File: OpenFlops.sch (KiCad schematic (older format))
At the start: 74 parts, among them P1 FLOPPY_CONN, P2 POWER_INPUT, P3 USB_A_FEMALE, P4 PROG_PORT, P5 JUMPERS, P6 ENCODER_PORT, P7 DISPLAY_PORT, Q1 MOS_N_GSD, Q2 MOS_N_GSD, Q3 MOS_N_GSD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

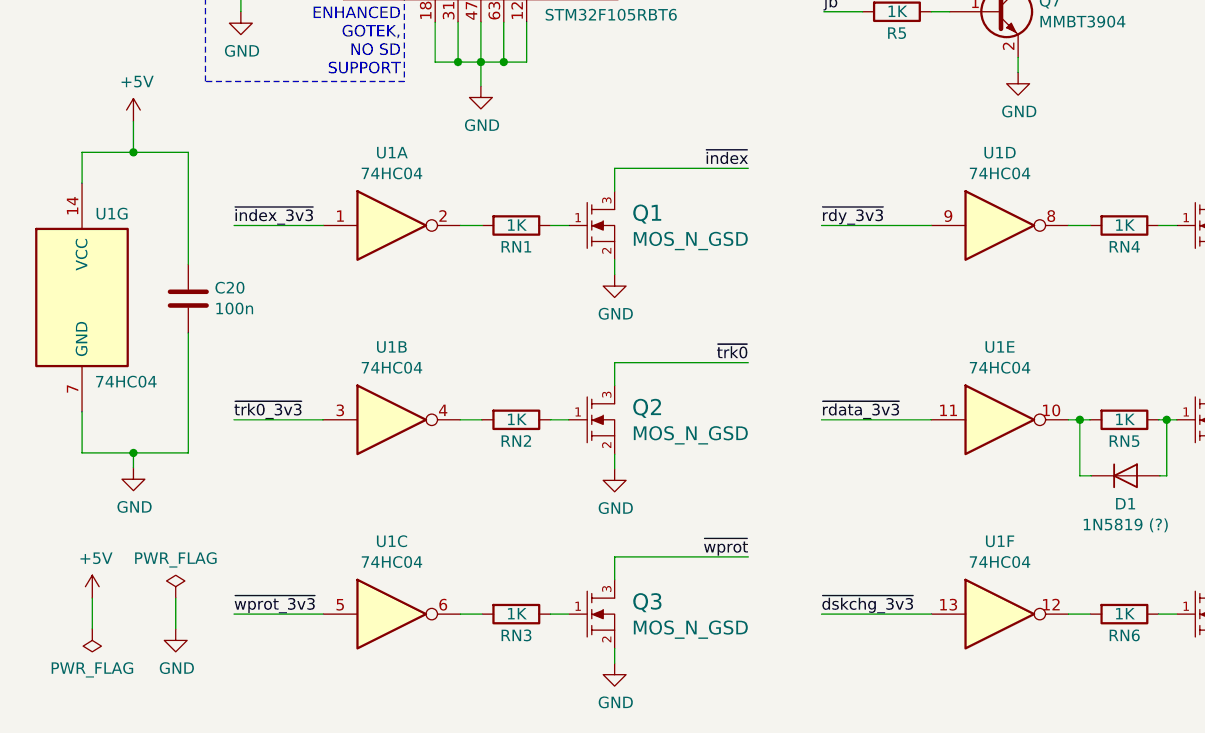
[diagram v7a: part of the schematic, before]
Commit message: 74HC04 -> 74HCT04
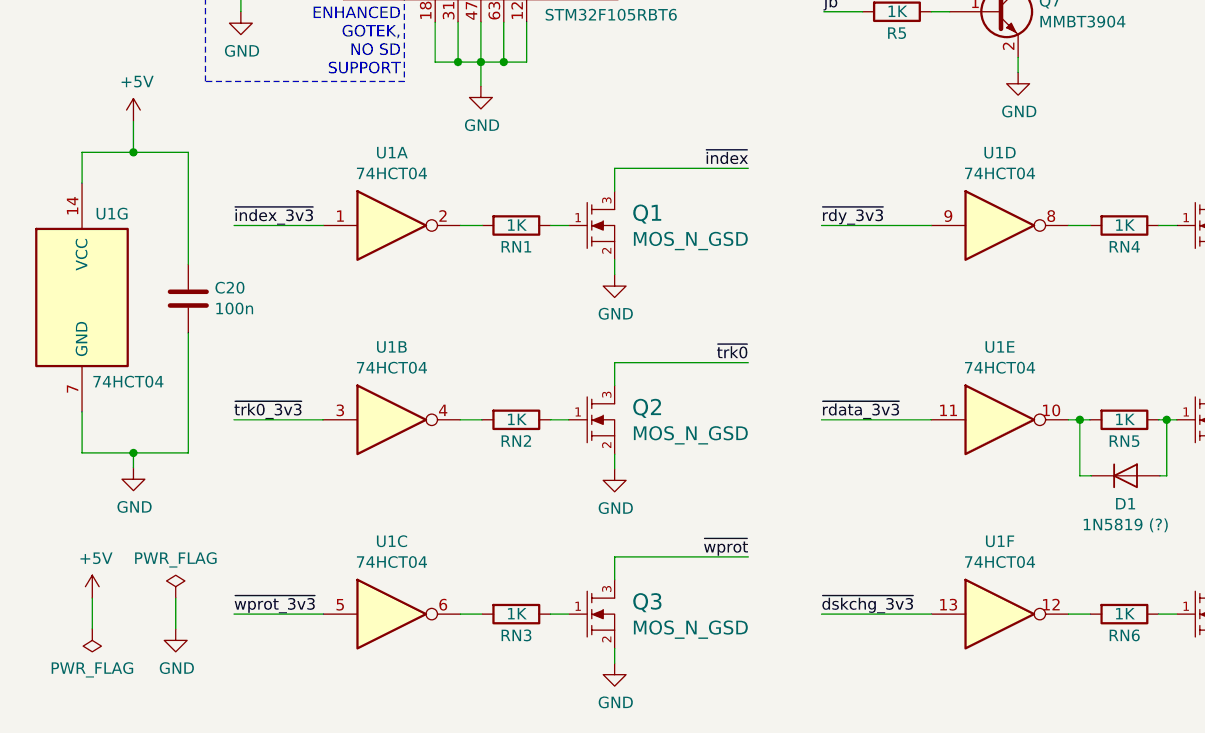
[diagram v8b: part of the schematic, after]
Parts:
- U1: value 74HC04 -> 74HCT04
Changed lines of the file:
@@
 P 2165 5590
 F 0 "U1" H 2165 5907 50  0000 C CNN
-F 1 "74HC04" H 2165 5816 50  0000 C CNN
+F 1 "74HCT04" H 2165 5816 50  0000 C CNN
 F 2 "Package_SO:SOIC-14_3.9x8.7mm_P1.27mm" H 2165 5590 50  0001 C CNN
 F 3 "https://assets.nexperia.com/documents/data-sheet/74HC_HCT04.pdf" H 2165 5590 50  0001 C CNN
@@
 P 2165 7290
 F 0 "U1" H 2165 7607 50  0000 C CNN
-F 1 "74HC04" H 2165 7516 50  0000 C CNN
+F 1 "74HCT04" H 2165 7516 50  0000 C CNN
 F 2 "Package_SO:SOIC-14_3.9x8.7mm_P1.27mm" H 2165 7290 50  0001 C CNN
 F 3 "https://assets.nexperia.com/documents/data-sheet/74HC_HCT04.pdf" H 2165 7290 50  0001 C CNN
@@
 P 4825 5590
 F 0 "U1" H 4825 5907 50  0000 C CNN
-F 1 "74HC04" H 4825 5816 50  0000 C CNN
+F 1 "74HCT04" H 4825 5816 50  0000 C CNN
 F 2 "Package_SO:SOIC-14_3.9x8.7mm_P1.27mm" H 4825 5590 50  0001 C CNN
 F 3 "https://assets.nexperia.com/documents/data-sheet/74HC_HCT04.pdf" H 4825 5590 50  0001 C CNN
@@
 P 4825 6440
 F 0 "U1" H 4825 6757 50  0000 C CNN
-F 1 "74HC04" H 4825 6666 50  0000 C CNN
+F 1 "74HCT04" H 4825 6666 50  0000 C CNN
 F 2 "Package_SO:SOIC-14_3.9x8.7mm_P1.27mm" H 4825 6440 50  0001 C CNN
 F 3 "https://assets.nexperia.com/documents/data-sheet/74HC_HCT04.pdf" H 4825 6440 50  0001 C CNN
@@
 P 4825 7290
 F 0 "U1" H 4825 7607 50  0000 C CNN
-F 1 "74HC04" H 4825 7516 50  0000 C CNN
+F 1 "74HCT04" H 4825 7516 50  0000 C CNN
 F 2 "Package_SO:SOIC-14_3.9x8.7mm_P1.27mm" H 4825 7290 50  0001 C CNN
 F 3 "https://assets.nexperia.com/documents/data-sheet/74HC_HCT04.pdf" H 4825 7290 50  0001 C CNN
@@
 P 810 5905
 F 0 "U1" H 1015 6270 50  0000 R CNN
-F 1 "74HC04" H 1140 5535 50  0000 R CNN
+F 1 "74HCT04" H 1170 5535 50  0000 R CNN
 F 2 "Package_SO:SOIC-14_3.9x8.7mm_P1.27mm" H 810 5905 50  0001 C CNN
 F 3 "https://assets.nexperia.com/documents/data-sheet/74HC_HCT04.pdf" H 810 5905 50  0001 C CNN
@@
 P 2165 6440
 F 0 "U1" H 2165 6757 50  0000 C CNN
-F 1 "74HC04" H 2165 6666 50  0000 C CNN
+F 1 "74HCT04" H 2165 6666 50  0000 C CNN
 F 2 "Package_SO:SOIC-14_3.9x8.7mm_P1.27mm" H 2165 6440 50  0001 C CNN
 F 3 "https://assets.nexperia.com/documents/data-sheet/74HC_HCT04.pdf" H 2165 6440 50  0001 C CNN
